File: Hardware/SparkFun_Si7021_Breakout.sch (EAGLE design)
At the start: 14 parts, among them U1 SI7021

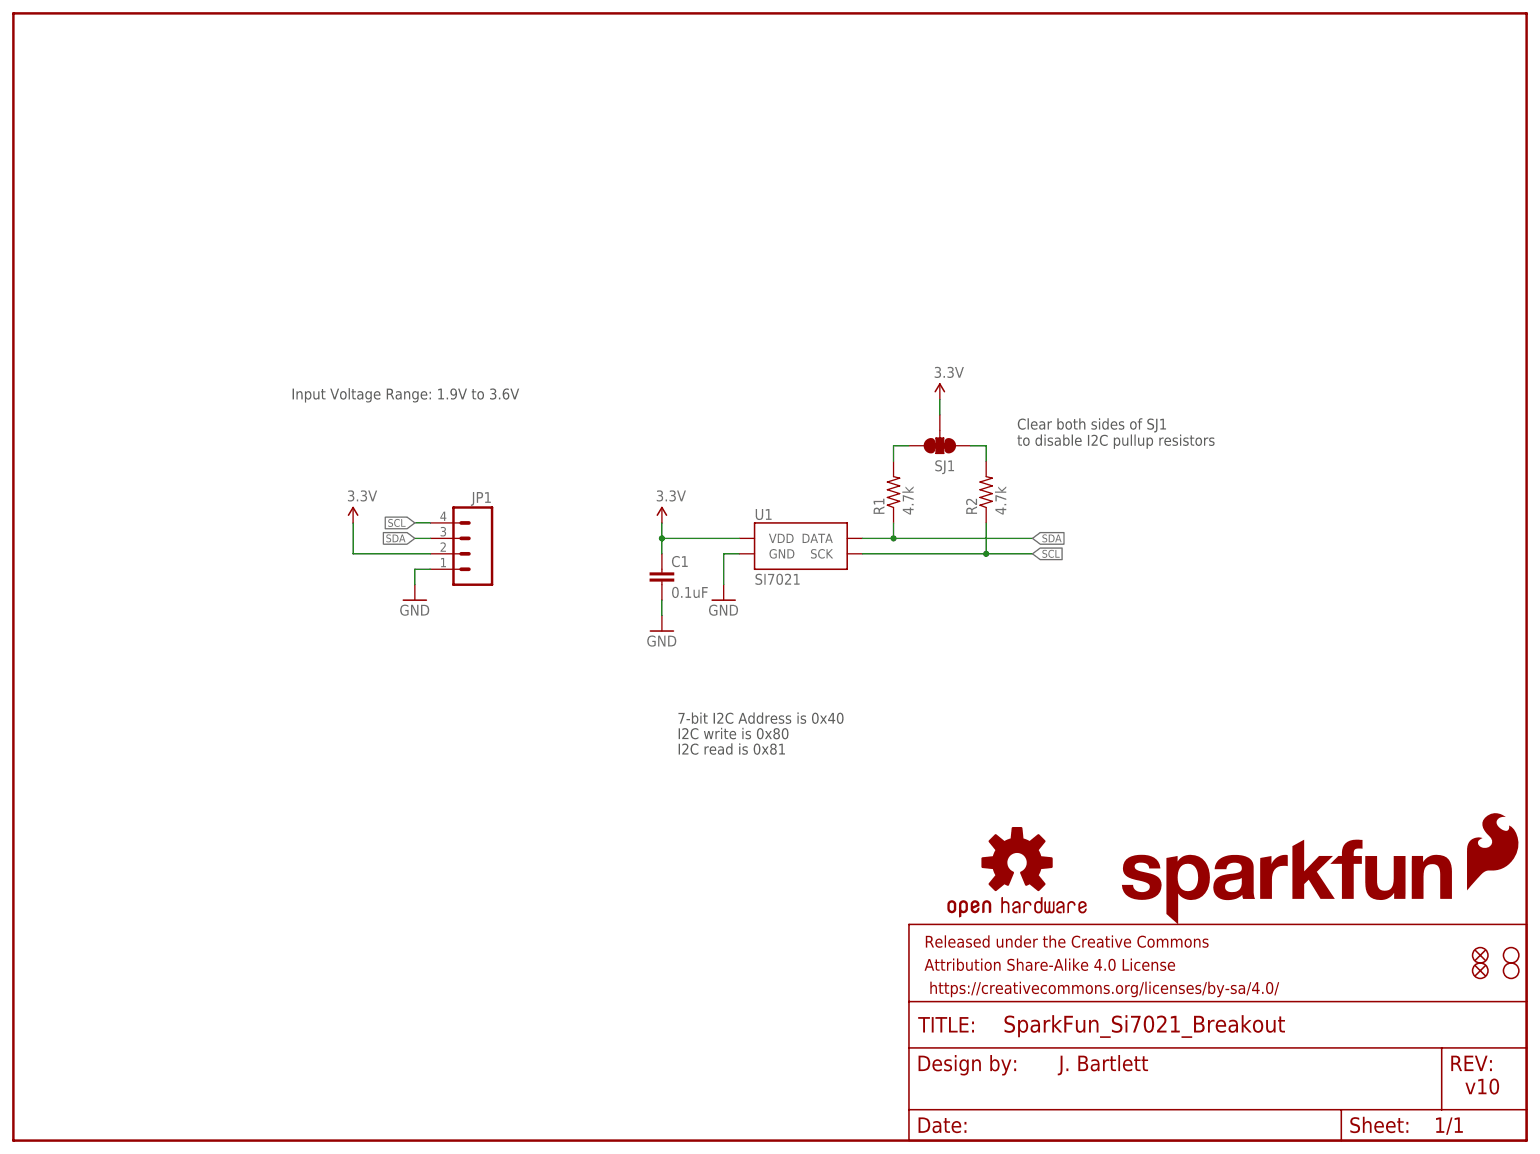
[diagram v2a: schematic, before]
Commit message: Pushing minor changes from first QC check
Caps and resistors needed prod ID, version should be v01, not v10,
altered center pad on Si7021 IC to have 50% paste instead of 100%.
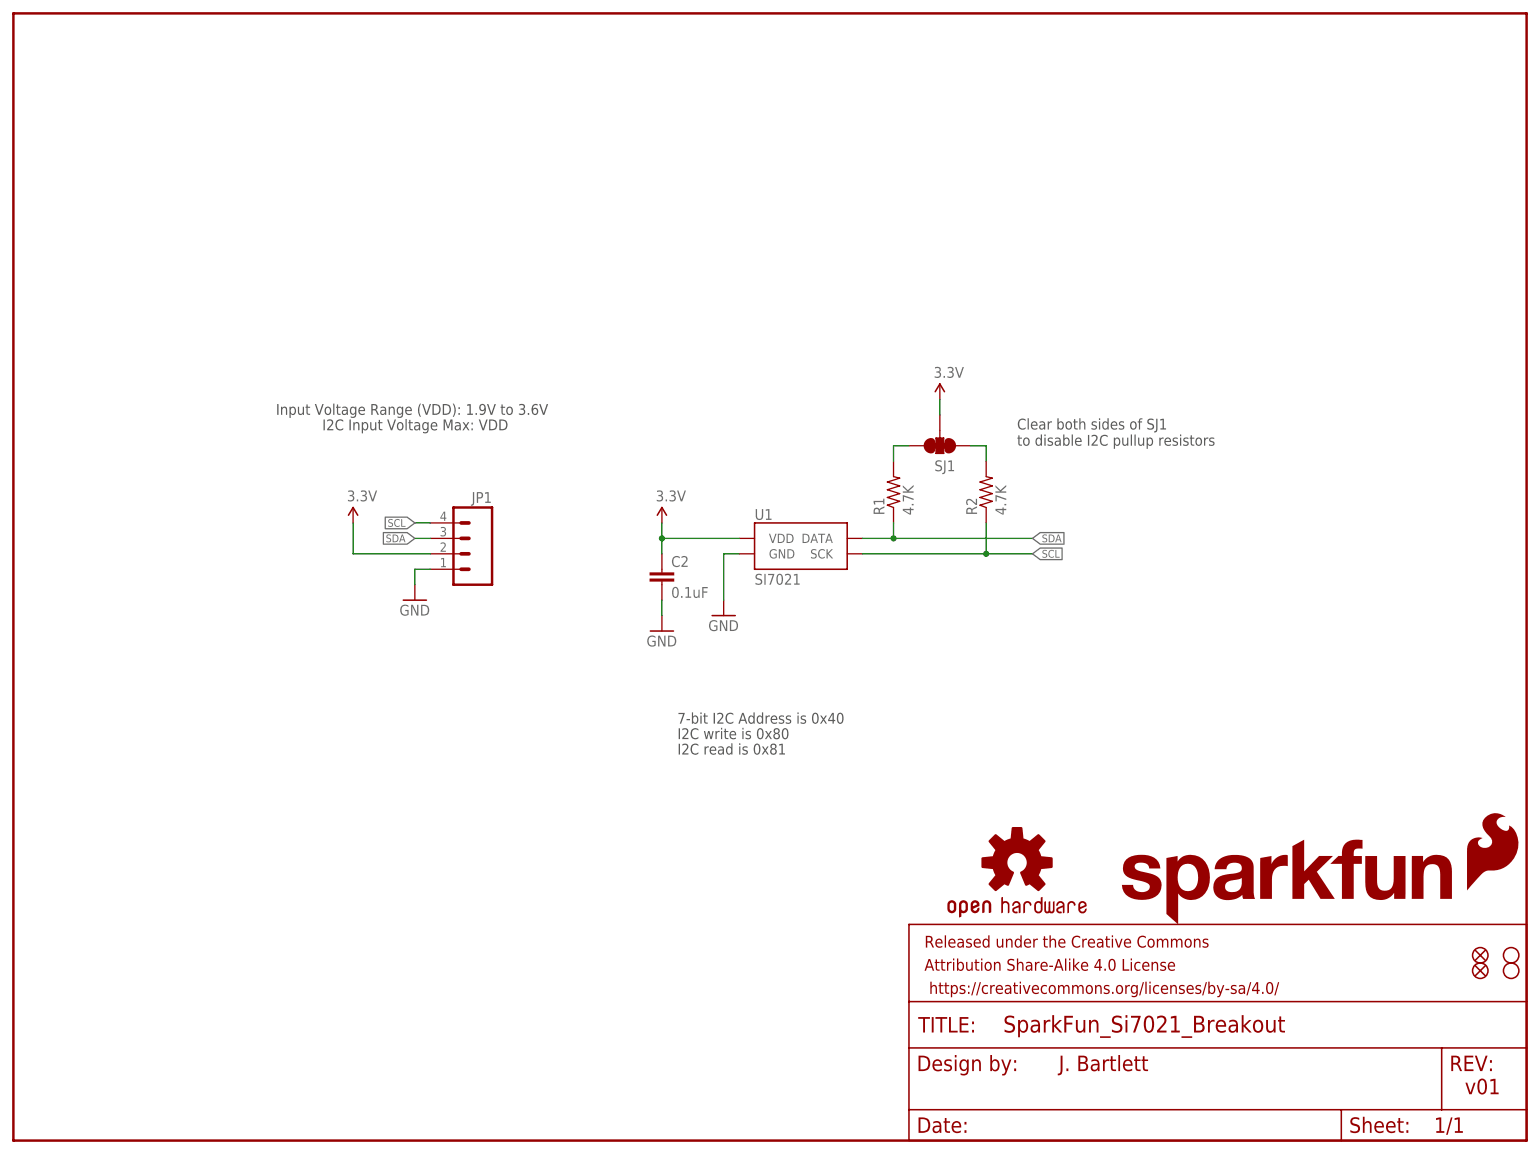
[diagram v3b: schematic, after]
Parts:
- removed C1: 0.1uF, SparkFun:CAP0603-CAP
- added C2: 0.1uF, SparkFun-Capacitors:0.1UF-25V(+80/-20%)(0603)
- R1, R2: value 4.7k -> 4.7K; device SparkFun:RESISTOR0603-RES -> SparkFun-Resistors:4.7KOHM-1/10W-1%(0603)
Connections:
- net 3.3V: now also C2.1; no longer C1.1
- net GND: now also C2.2; no longer C1.2
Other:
- note added: "I2C Input Voltage Max: VDD"
- note added: "Input Voltage Range (VDD): 1.9V to 3.6V"
- note added: "v01"
- note removed: "Input Voltage Range: 1.9V to 3.6V"
- note removed: "v10"
